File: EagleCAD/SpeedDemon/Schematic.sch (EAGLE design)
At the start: 51 parts, among them Q1 DMC2700, U1 LM3676, U3 STM32F072-LQFP48

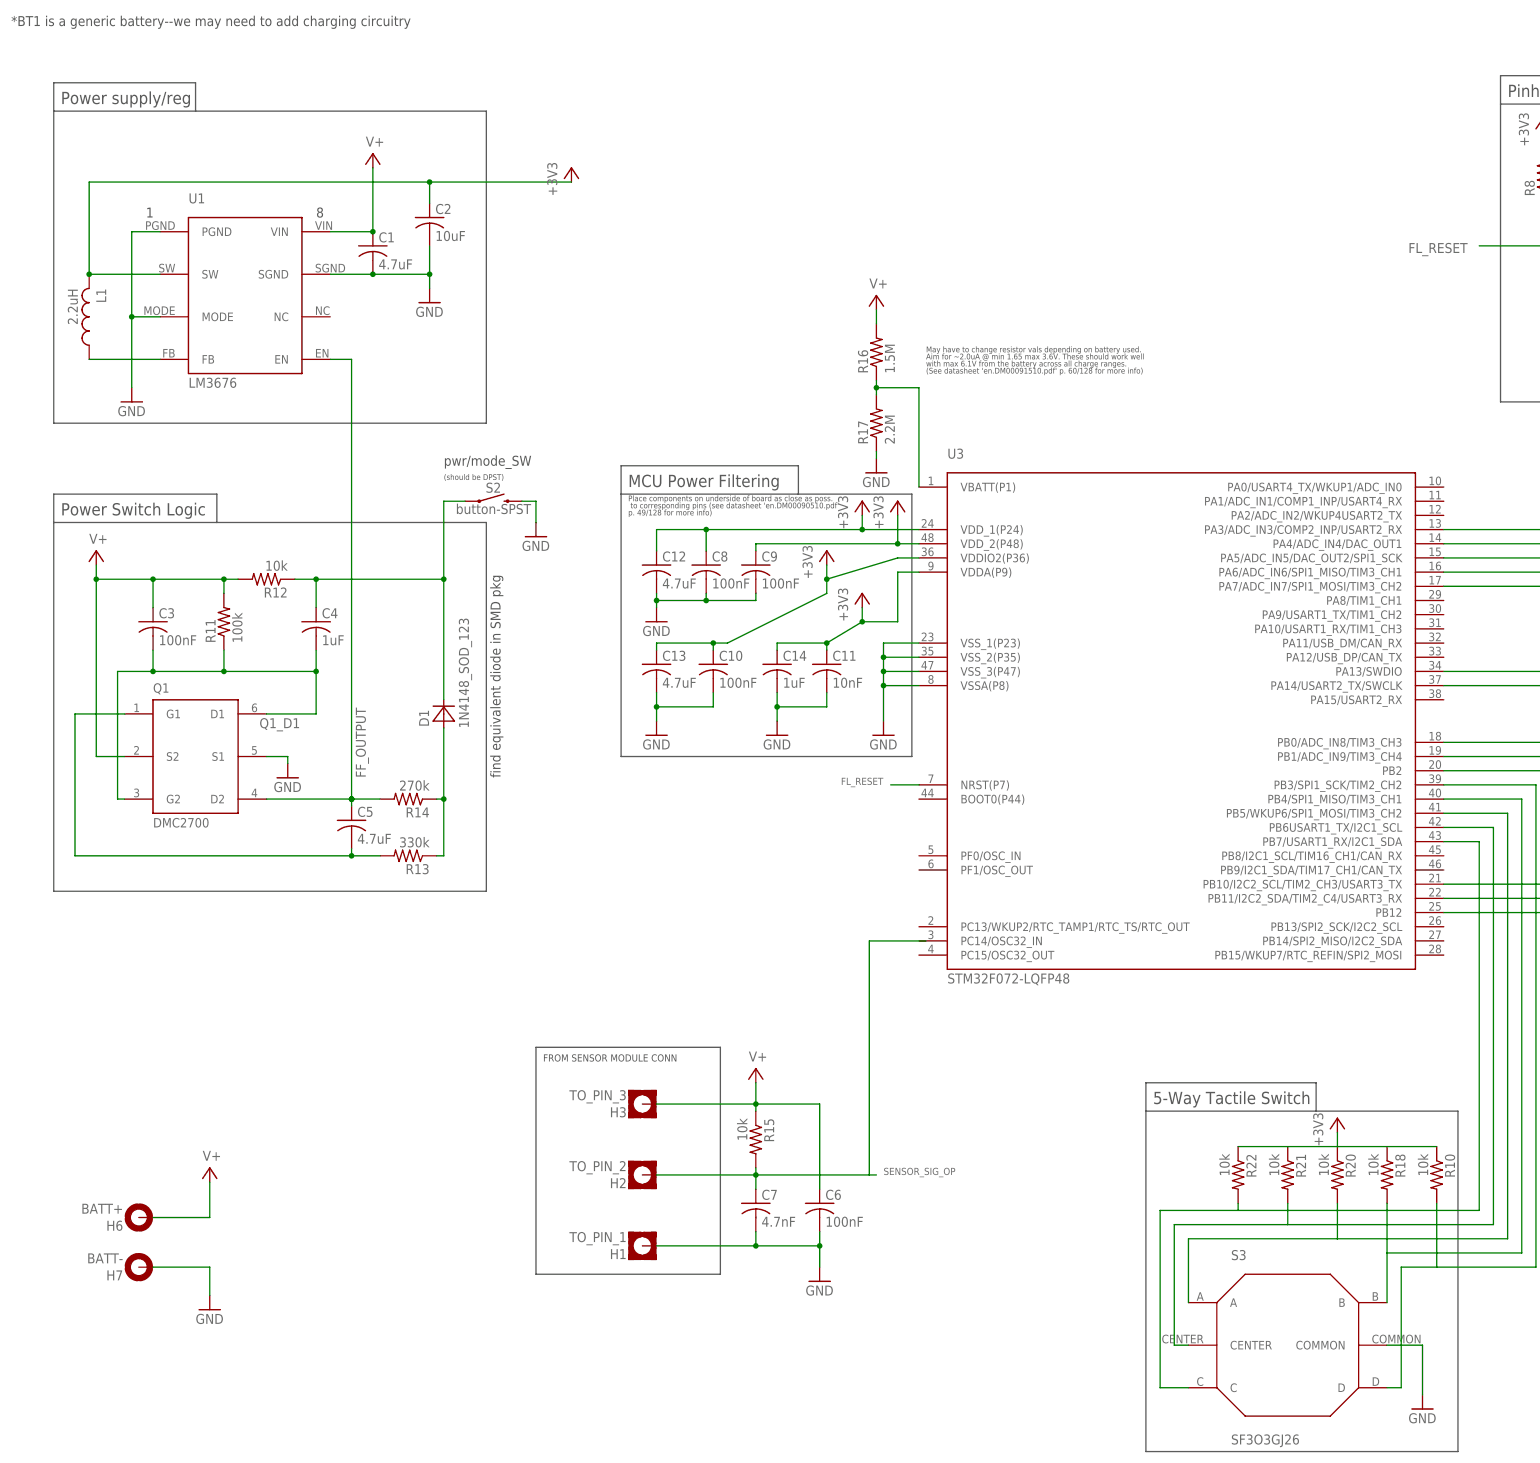
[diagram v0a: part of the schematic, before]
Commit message: Power section of schematic finished. Some parts added to libraries.
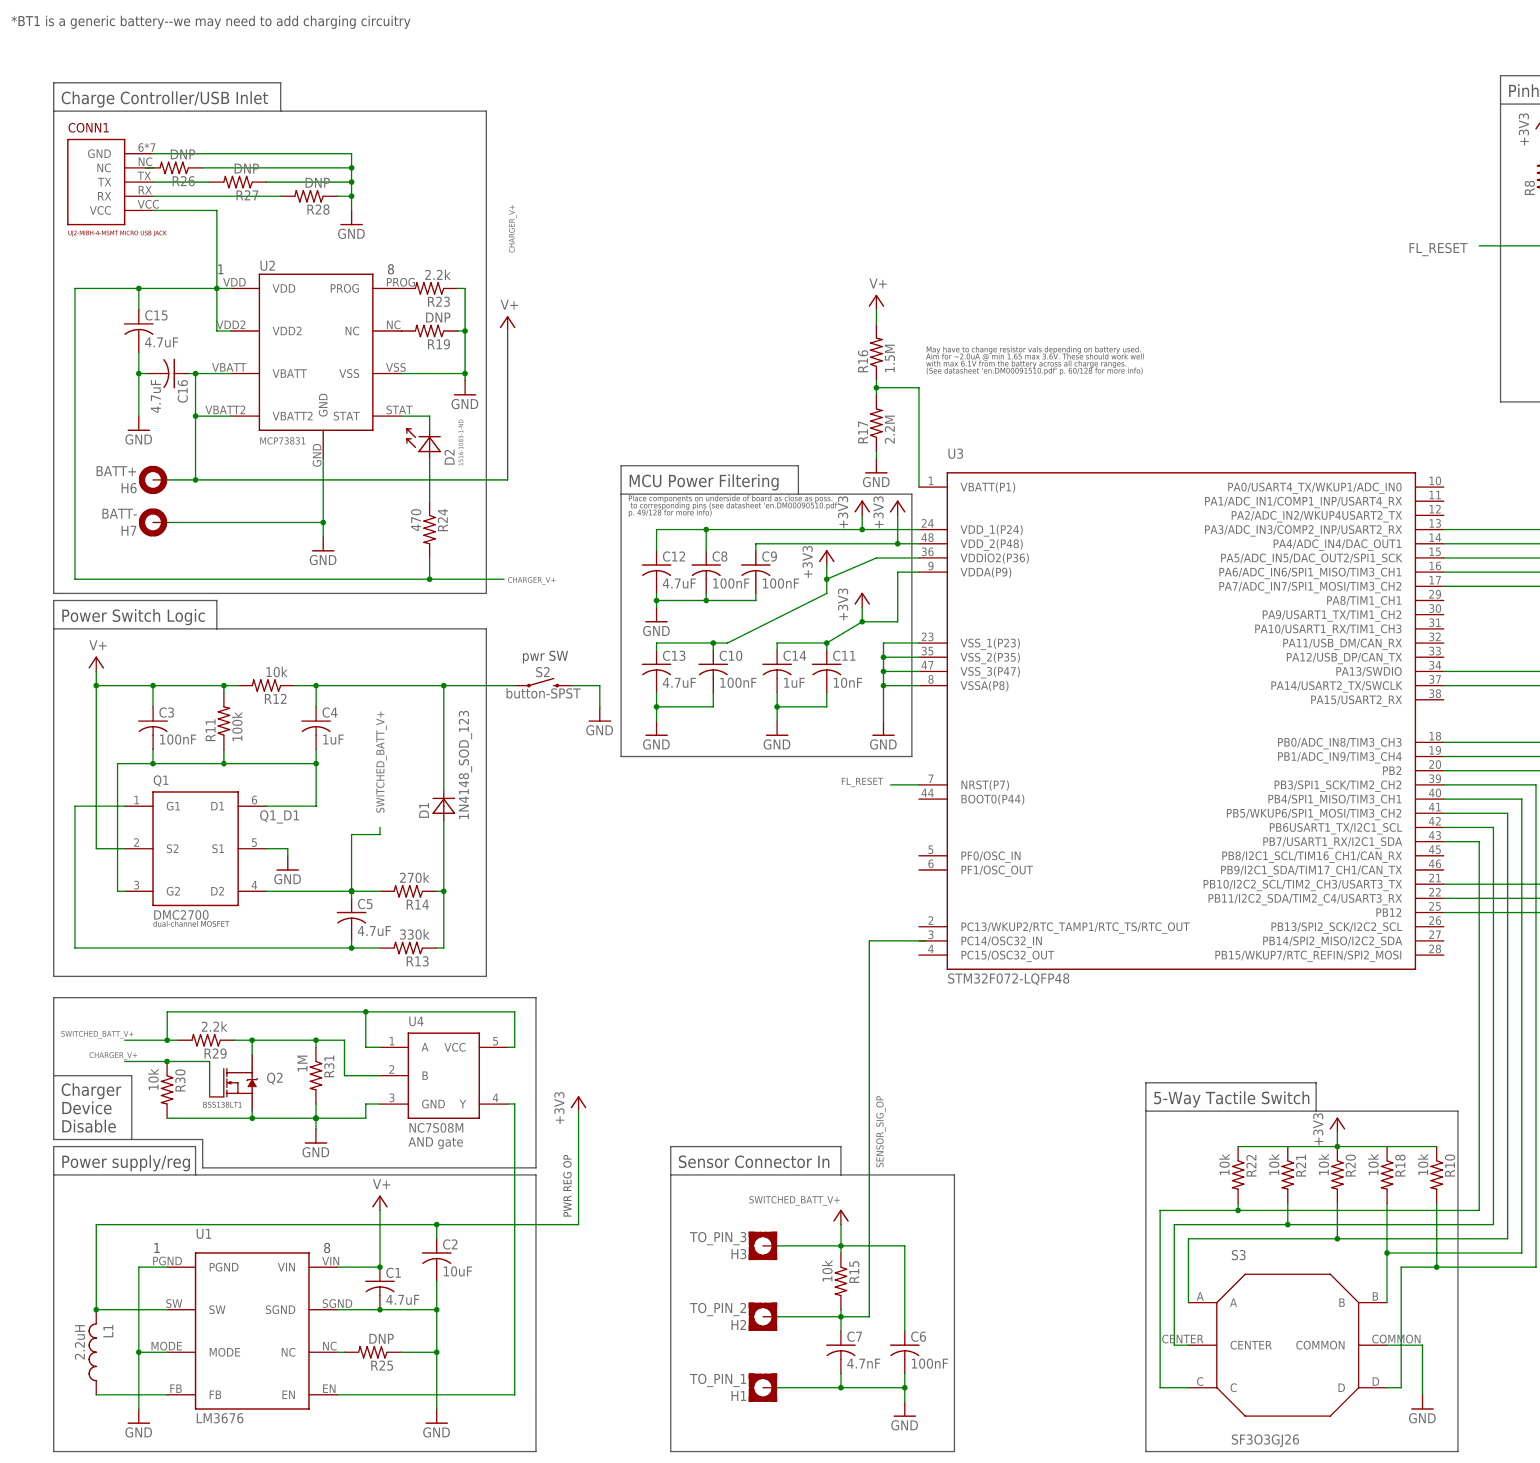
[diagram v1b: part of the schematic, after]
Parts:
- added C15, C16: 4.7uF, 0805_generics:C_0805_NP
- added CONN1: (no value), USB_jack_102-4008-1-ND:USB-MICRO-B
- added D2: (no value), LCRD_SMD_generics:LED_0805
- added Q2: (no value), DMC2700:BSS138LT1_TO-236
- added R19, R25, R26, R27, R28: DNP, 0805_generics:R_0805
- added R23, R29: 2.2k, 0805_generics:R_0805
- added R24: 470, 0805_generics:R_0805
- added R30: 10k, 0805_generics:R_0805
- added R31: 1M, 0805_generics:R_0805
- added U2: (no value), mcp73831:MCP73831_8-DFN
- added U4: (no value), DMC2700:NC7S08_SOT_23_5
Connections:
- removed net FF_OUTPUT: C5.1, Q1.D2, R14.2, U1.EN
- new net CHARGER_V+: C15.1, CONN1.VCC, Q2.G, R24.2, R30.1, U2.VDD, U2.VDD2
- new net N$28: Q2.D, R29.1, R31.1, U4.B
- new net N$31: D2.C, U2.STAT
- new net N$32: R19.2, U2.NC
- new net N$33: D2.A, R24.1
- new net N$34: R23.2, U2.PROG
- new net N$35: R25.2, U1.NC
- new net N$36: CONN1.NC, R26.2
- new net N$37: U1.EN, U4.Y
- new net N$38: CONN1.TX, R27.2
- new net N$39: CONN1.RX, R28.2
- new net SWITCHED_BATT_V+: C5.1, C6.1, H3.MOUNT, Q1.D2, R14.2, R15.1, R29.2, U4.A, U4.VCC
- net GND: now also C15.2, C16.2, CONN1.GND, Q2.S, R19.1, R23.1, R25.1, R26.1, R27.1, R28.1, R30.2, R31.2, U2.GND, U2.VSS, U4.GND
- net V+: now also C16.1, U2.VBATT, U2.VBATT2; no longer C6.1, H3.MOUNT, R15.1
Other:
- note added: "BSS138LT1"
- note added: "Charge Controller/USB Inlet"
- note added: "Charger Device Disable"
- note added: "PWR REG OP"
- note added: "Sensor Connector In"
- note added: "dual-channel MOSFET"
- note added: "pwr SW"
- note removed: "(should be DPST)"
- note removed: "FROM SENSOR MODULE CONN"
- note removed: "find equivalent diode in SMD pkg"
- note removed: "pwr/mode_SW"
- moved on the sheet: C1, C2, C3, C4, C5, C6, C7, D1, H1, H2, H3, H6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

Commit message: Schematic update, passed ERC. Added second page with sensor module. Added several parts libraries.
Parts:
- removed C6: 100nF, 0805_generics:C_0805_NP
- removed R21: 10k, 0805_generics:R_0805
- removed S2: button-SPST, SparkFun-Switches:MOMENTARY-SWITCH-SPST-PTH-6.0MM
- added C17: 100nF, rcl:C-US025-024X044
- added R32: 10k, 0805_generics:R_0805
- added SIGNAL_OP: (no value), wirepad:1,6/0,8
- added U5: (no value), US5881:US5881
- TM1: value (none) -> 10k
- U1: value LM3676 -> (none); device LM3676:LM3676 -> mcp73831:MCP73831_8-DFN
- U2: device mcp73831:MCP73831_8-DFN -> DMC2700:NC7S08_SOT_23_5
- U3: value STM32F072-LQFP48 -> LM3676; device stm32f0:STM32F072-LQFP48 -> LM3676:LM3676
- U4: value (none) -> STM32F072-LQFP48; device DMC2700:NC7S08_SOT_23_5 -> stm32f0:STM32F072-LQFP48
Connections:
- removed net CHARGER_V+: C15.1, CONN1.VCC, Q2.G, R24.2, R30.1, U2.VDD, U2.VDD2
- removed net N$11: C4.1, D1.C, R12.1, S2.1
- removed net N$26: R21.2, S3.CENTER, U3.PB6USART1_TX/I2C1_SCL
- removed net SWITCHED_BATT_V+: C5.1, C6.1, H3.MOUNT, Q1.D2, R14.2, R15.1, R29.2, U4.A, U4.VCC
- removed net V+: C1.1, C16.1, C3.1, H6.MOUNT, Q1.S2, R11.2, R12.2, R16.2, U1.VIN, U2.VBATT, U2.VBATT2
- new net +V+_CHG: C15.1, CONN1.VCC, Q2.G, R24.2, R30.1, U1.VDD, U1.VDD2
- new net BATT_CHG_LOGIC_OP: R32.1, U2.Y, U3.EN
- new net PWR_SW: C4.1, D1.C, R12.1, S3.CENTER
- new net VBATT+: C1.1, C16.1, C3.1, H6.MOUNT, Q1.S2, R11.2, R12.2, R16.2, U1.VBATT, U1.VBATT2, U3.VIN
- new net VBATT+_SW: C17.1, C5.1, H3.MOUNT, Q1.D2, R14.2, R15.1, R29.2, U2.A, U2.VCC, U5.VDD
- net +3V3: now also U3.SW, U4.VDDA(P9), U4.VDDIO2(P36), U4.VDD_1(P24), U4.VDD_2(P48); no longer R21.1, U1.SW, U3.VDDA(P9), U3.VDDIO2(P36), U3.VDD_1(P24), U3.VDD_2(P48)
- net FL_RESET: now also U4.NRST(P7); no longer U3.NRST(P7)
- net FL_SWCLK: now also U4.PA14/USART2_TX/SWCLK; no longer U3.PA14/USART2_TX/SWCLK
- net FL_SWDIO: now also U4.PA13/SWDIO; no longer U3.PA13/SWDIO
- net GND: now also C17.2, R32.2, U1.GND, U1.VSS, U3.MODE, U3.PGND, U3.SGND, U4.VSSA(P8), U4.VSS_1(P23), U4.VSS_2(P35), U4.VSS_3(P47), U5.VSS; no longer C6.2, S2.2, U1.MODE, U1.PGND, U1.SGND, U2.VSS, U3.VSSA(P8), U3.VSS_1(P23), U3.VSS_2(P35), U3.VSS_3(P47), U4.GND
- net N$10: now also U3.FB; no longer U1.FB
- net N$12: now also U4.PB0/ADC_IN8/TIM3_CH3; no longer U3.PB0/ADC_IN8/TIM3_CH3
- net N$13: now also U4.PB1/ADC_IN9/TIM3_CH4; no longer U3.PB1/ADC_IN9/TIM3_CH4
- net N$16: now also U4.PA3/ADC_IN3/COMP2_INP/USART2_RX; no longer U3.PA3/ADC_IN3/COMP2_INP/USART2_RX
- net N$17: now also U4.PA4/ADC_IN4/DAC_OUT1; no longer U3.PA4/ADC_IN4/DAC_OUT1
- net N$18: now also U4.PA5/ADC_IN5/DAC_OUT2/SPI1_SCK; no longer U3.PA5/ADC_IN5/DAC_OUT2/SPI1_SCK
- net N$19: now also U4.PA6/ADC_IN6/SPI1_MISO/TIM3_CH1; no longer U3.PA6/ADC_IN6/SPI1_MISO/TIM3_CH1
- net N$20: now also U4.PA7/ADC_IN7/SPI1_MOSI/TIM3_CH2; no longer U3.PA7/ADC_IN7/SPI1_MOSI/TIM3_CH2
- net N$21: now also U4.PB2; no longer U3.PB2
- net N$22: now also U4.PB10/I2C2_SCL/TIM2_CH3/USART3_TX; no longer U3.PB10/I2C2_SCL/TIM2_CH3/USART3_TX
- net N$23: now also U4.PB11/I2C2_SDA/TIM2_C4/USART3_RX; no longer U3.PB11/I2C2_SDA/TIM2_C4/USART3_RX
- net N$24: now also U4.PB12; no longer U3.PB12
- net N$25: now also U4.PB7/USART1_RX/I2C1_SDA; no longer U3.PB7/USART1_RX/I2C1_SDA
- net N$27: now also U4.PB5/WKUP6/SPI1_MOSI/TIM3_CH2; no longer U3.PB5/WKUP6/SPI1_MOSI/TIM3_CH2
- net N$28: now also U2.B; no longer U4.B
- net N$29: now also U4.PB4/SPI1_MISO/TIM3_CH1; no longer U3.PB4/SPI1_MISO/TIM3_CH1
- net N$30: now also U4.PB3/SPI1_SCK/TIM2_CH2; no longer U3.PB3/SPI1_SCK/TIM2_CH2
- net N$31: now also U1.STAT; no longer U2.STAT
- net N$32: now also U1.NC; no longer U2.NC
- net N$34: now also U1.PROG; no longer U2.PROG
- net N$35: now also U3.NC; no longer U1.NC
- net N$37: now also SIGNAL_OP.P, U5.OP; no longer U1.EN, U4.Y
- net N$7: now also U4.VBATT(P1); no longer U3.VBATT(P1)
- net SENSOR_SIG_OP: now also U4.PC14/OSC32_IN
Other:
- note added: "'Speed Demon' Hall Effect Speedometer"
- note added: "*NOTE: No PCB for this portion of circuit! Use point-to-point wiring."
- note added: "3-Conductor cable run"
- note added: "Main PCB"
- note added: "PWR REG OP (Main Device Power)"
- note added: "Pads connect to Mini XLR-M chassis mount conn"
- note added: "See p. 2 for sensor module schematic"
- note added: "Sensor module"
- note added: "Use Mogami W2944 Balanced Console Cable or similar (tie gnd to cable shield)"
- note added: "XLR-F Cable0 mount conn"
- note removed: "PWR REG OP"
- note removed: "pwr SW"

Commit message: tiny edits
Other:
- note removed: "*BT1 is a generic battery--we may need to add charging circuitry"
- moved on the sheet: Q2
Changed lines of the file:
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@@
 </classes>
 <parts>
-<part name="FRAME1" library="frames" library_urn="urn:adsk.eagle:library:229" deviceset="A3L-LOC" device=""/>
+<part name="FRAME1" library="frames" library_urn="urn:adsk.eagle:library:229" deviceset="A3L-LOC" device="" value=" "/>
 <part name="U4" library="stm32f0" deviceset="STM32F072" device="-LQFP48"/>
 <part name="JP1" library="pinhead" library_urn="urn:adsk.eagle:library:325" deviceset="PINHD-2X5" device="" package3d_urn="urn:adsk.eagle:package:22470/2"/>
@@
 <wire x1="93.98" y1="7.62" x2="7.62" y2="7.62" width="0.1524" layer="97"/>
 <text x="8.89" y="58.42" size="2.1844" layer="97">Power supply/reg</text>
-<text x="0" y="262.89" size="1.778" layer="97">*BT1 is a generic battery--we may need to add charging circuitry</text>
 <wire x1="7.62" y1="62.23" x2="33.02" y2="62.23" width="0.1524" layer="97"/>
 <wire x1="33.02" y1="62.23" x2="33.02" y2="57.15" width="0.1524" layer="97"/>
@@
 <instance part="GND5" gate="1" x="22.86" y="12.7"/>
 <instance part="GND6" gate="1" x="76.2" y="12.7"/>
-<instance part="+3V4" gate="G$1" x="108.585" y="246.38"/>
+<instance part="+3V4" gate="G$1" x="106.045" y="246.38"/>
 <instance part="L1" gate="G$1" x="15.24" y="25.4" rot="R180"/>
 <instance part="C1" gate="G$1" x="66.04" y="38.1"/>
@@
 <instance part="GND21" gate="1" x="60.96" y="227.33"/>
 <instance part="C16" gate="G$1" x="29.21" y="200.66" rot="R270"/>
-<instance part="Q2" gate="G$1" x="40.6146" y="73.66"/>
+<instance part="Q2" gate="G$1" x="40.6146" y="74.295"/>
 <instance part="R29" gate="G$1" x="34.925" y="81.28" rot="R180"/>
 <instance part="GND15" gate="1" x="54.5846" y="62.865"/>
@@
 <attribute name="VALUE" x="61.595" y="53.975" size="1.778" layer="96"/>
 </instance>
-<instance part="VBATT_SW1" gate="G$1" x="100.33" y="242.57" smashed="yes">
-<attribute name="VALUE" x="98.425" y="229.235" size="1.778" layer="96" rot="R90"/>
+<instance part="VBATT_SW1" gate="G$1" x="97.79" y="242.57" smashed="yes">
+<attribute name="VALUE" x="95.885" y="229.235" size="1.778" layer="96" rot="R90"/>
 </instance>
-<instance part="VBATT+2" gate="G$1" x="92.71" y="246.38"/>
+<instance part="VBATT+2" gate="G$1" x="91.44" y="246.38"/>
 <instance part="VBATT+3" gate="G$1" x="15.24" y="148.59"/>
 <instance part="VBATT+4" gate="G$1" x="154.94" y="214.63"/>
@@
 <wire x1="76.2" y1="48.26" x2="76.2" y2="51.435" width="0.1524" layer="91"/>
 <wire x1="76.2" y1="51.435" x2="106.045" y2="51.435" width="0.1524" layer="91"/>
-<wire x1="106.045" y1="51.435" x2="106.045" y2="189.865" width="0.1524" layer="91"/>
-<wire x1="106.045" y1="189.865" x2="108.585" y2="189.865" width="0.1524" layer="91"/>
-<wire x1="108.585" y1="189.865" x2="108.585" y2="243.84" width="0.1524" layer="91"/>
+<wire x1="106.045" y1="51.435" x2="106.045" y2="243.84" width="0.1524" layer="91"/>
 <pinref part="C2" gate="G$1" pin="1"/>
 <wire x1="76.2" y1="45.72" x2="76.2" y2="48.26" width="0.1524" layer="91"/>
@@
 <wire x1="63.5" y1="69.85" x2="66.04" y2="69.85" width="0.1524" layer="91"/>
 <pinref part="R30" gate="G$1" pin="2"/>
-<wire x1="27.9146" y1="67.31" x2="43.1546" y2="67.31" width="0.1524" layer="91"/>
+<wire x1="54.5846" y1="67.31" x2="43.18" y2="67.31" width="0.1524" layer="91"/>
 <pinref part="Q2" gate="G$1" pin="S"/>
-<wire x1="43.18" y1="67.31" x2="54.5846" y2="67.31" width="0.1524" layer="91"/>
-<wire x1="43.1546" y1="68.58" x2="43.1546" y2="67.31" width="0.1524" layer="91"/>
-<wire x1="43.1546" y1="67.31" x2="43.18" y2="67.31" width="0.1524" layer="91"/>
+<wire x1="43.18" y1="67.31" x2="27.9146" y2="67.31" width="0.1524" layer="91"/>
+<wire x1="43.18" y1="67.31" x2="43.18" y2="69.215" width="0.1524" layer="91"/>
+<wire x1="43.18" y1="69.215" x2="43.1546" y2="69.215" width="0.1524" layer="91"/>
 <junction x="43.18" y="67.31"/>
 </segment>
@@
 <wire x1="210.82" y1="26.67" x2="198.755" y2="26.67" width="0.1524" layer="91"/>
 <wire x1="198.755" y1="26.67" x2="198.755" y2="64.77" width="0.1524" layer="91"/>
-<wire x1="198.755" y1="64.77" x2="97.155" y2="64.77" width="0.1524" layer="91"/>
-<wire x1="97.155" y1="64.77" x2="97.155" y2="144.78" width="0.1524" layer="91"/>
-<wire x1="77.47" y1="144.78" x2="97.155" y2="144.78" width="0.1524" layer="91"/>
+<wire x1="198.755" y1="64.77" x2="99.695" y2="64.77" width="0.1524" layer="91"/>
+<wire x1="99.695" y1="64.77" x2="99.695" y2="92.71" width="0.1524" layer="91"/>
+<wire x1="99.695" y1="92.71" x2="88.9" y2="92.71" width="0.1524" layer="91"/>
+<wire x1="88.9" y1="92.71" x2="88.9" y2="144.78" width="0.1524" layer="91"/>
+<wire x1="77.47" y1="144.78" x2="88.9" y2="144.78" width="0.1524" layer="91"/>
 <junction x="77.47" y="144.78"/>
-<label x="96.52" y="135.89" size="1.4224" layer="95" rot="R90"/>
+<label x="90.805" y="136.525" size="1.4224" layer="95" rot="R90"/>
+<label x="197.485" y="66.675" size="1.778" layer="95" rot="R180"/>
 </segment>
 </net>
@@
 <wire x1="40.005" y1="81.28" x2="43.1546" y2="81.28" width="0.1524" layer="91"/>
 <pinref part="Q2" gate="G$1" pin="D"/>
-<wire x1="43.1546" y1="81.28" x2="43.1546" y2="78.74" width="0.1524" layer="91"/>
+<wire x1="43.1546" y1="81.28" x2="43.1546" y2="79.375" width="0.1524" layer="91"/>
 <wire x1="43.1546" y1="81.28" x2="54.5846" y2="81.28" width="0.1524" layer="91"/>
 <junction x="43.1546" y="81.28"/>
@@
 <segment>
 <pinref part="R14" gate="G$1" pin="2"/>
-<wire x1="60.96" y1="107.95" x2="60.96" y2="118.11" width="0.1524" layer="91"/>
+<wire x1="60.96" y1="107.95" x2="60.96" y2="115.57" width="0.1524" layer="91"/>
 <wire x1="60.96" y1="107.95" x2="66.04" y2="107.95" width="0.1524" layer="91"/>
 <junction x="60.96" y="107.95"/>
@@
 <wire x1="60.96" y1="106.68" x2="60.96" y2="107.95" width="0.1524" layer="91"/>
 <junction x="60.96" y="107.95"/>
-<wire x1="60.96" y1="118.11" x2="100.33" y2="118.11" width="0.1524" layer="91"/>
-<wire x1="100.33" y1="118.11" x2="100.33" y2="240.03" width="0.1524" layer="91"/>
+<wire x1="60.96" y1="115.57" x2="97.79" y2="115.57" width="0.1524" layer="91"/>
+<wire x1="97.79" y1="115.57" x2="97.79" y2="240.03" width="0.1524" layer="91"/>
 <pinref part="VBATT_SW1" gate="G$1" pin="VBATT+_SW"/>
 </segment>
@@
 <segment>
 <pinref part="Q2" gate="G$1" pin="G"/>
-<wire x1="35.5346" y1="71.12" x2="35.5346" y2="77.47" width="0.1524" layer="91"/>
+<wire x1="35.5346" y1="71.755" x2="35.5346" y2="77.47" width="0.1524" layer="91"/>
 <pinref part="R30" gate="G$1" pin="1"/>
 <wire x1="35.5346" y1="77.47" x2="27.9146" y2="77.47" width="0.1524" layer="91"/>
@@
 <wire x1="33.02" y1="181.61" x2="33.02" y2="193.04" width="0.1524" layer="91"/>
 <junction x="33.02" y="193.04"/>
-<wire x1="33.02" y1="181.61" x2="92.71" y2="181.61" width="0.1524" layer="91"/>
-<wire x1="92.71" y1="181.61" x2="92.71" y2="243.84" width="0.1524" layer="91"/>
+<wire x1="33.02" y1="181.61" x2="91.44" y2="181.61" width="0.1524" layer="91"/>
+<wire x1="91.44" y1="181.61" x2="91.44" y2="243.84" width="0.1524" layer="91"/>
 <junction x="33.02" y="181.61"/>
 <pinref part="VBATT+2" gate="G$1" pin="VBATT+"/>
